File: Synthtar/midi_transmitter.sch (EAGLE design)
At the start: 7 parts, among them IC4 4081N

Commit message: misc changes
misc updates while doing documentation
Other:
- note added: "^ according to the docs I actually do not, cool"
- note added: "need to invert this first! optocoupler inverts on the other side"
- note removed: "according to the docs I actually do not, cool"
- note removed: "need to invert this first!~ optocoupler inverts on the other side"
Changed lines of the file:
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@@
 <text x="93.98" y="10.16" size="1.778" layer="91">thinking about replacing this midi jack with usb midi functionality</text>
 <text x="96.52" y="5.08" size="1.778" layer="97">or having both!</text>
-<text x="20.32" y="43.18" size="1.778" layer="91">need to invert this first!~ optocoupler inverts on the other side</text>
+<text x="20.32" y="48.26" size="1.778" layer="91">need to invert this first! optocoupler inverts on the other side</text>
 <text x="22.86" y="55.88" size="1.778" layer="91">tie all inputs together to avoid floating?</text>
 <text x="68.58" y="-10.16" size="1.778" layer="91">can't drive from nand because my nands can't source enough current!</text>
@@
 <text x="132.08" y="-20.32" size="1.778" layer="91">uses 2.8mA max, 1.7mA avg</text>
 <text x="-10.16" y="68.58" size="1.778" layer="91">just go with what you have for now, you're running out of time</text>
-<text x="20.32" y="45.72" size="1.778" layer="91">according to the docs I actually do not, cool</text>
+<text x="20.32" y="45.72" size="1.778" layer="91">^ according to the docs I actually do not, cool</text>
 <text x="33.02" y="10.16" size="1.778" layer="91">less than 1mA idle current, about 7mA when transmitting</text>
 <text x="33.02" y="7.62" size="1.778" layer="91">(5v-2v)/(220+220 (other side))=6.8mA</text>

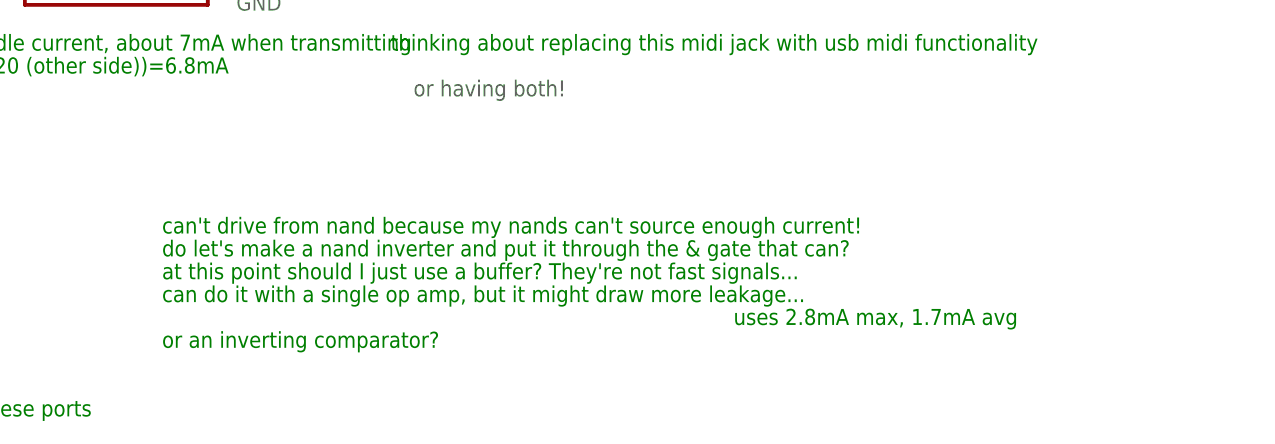
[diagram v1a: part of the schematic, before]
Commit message: deleted some comments
deleted comments in midi trasmitter
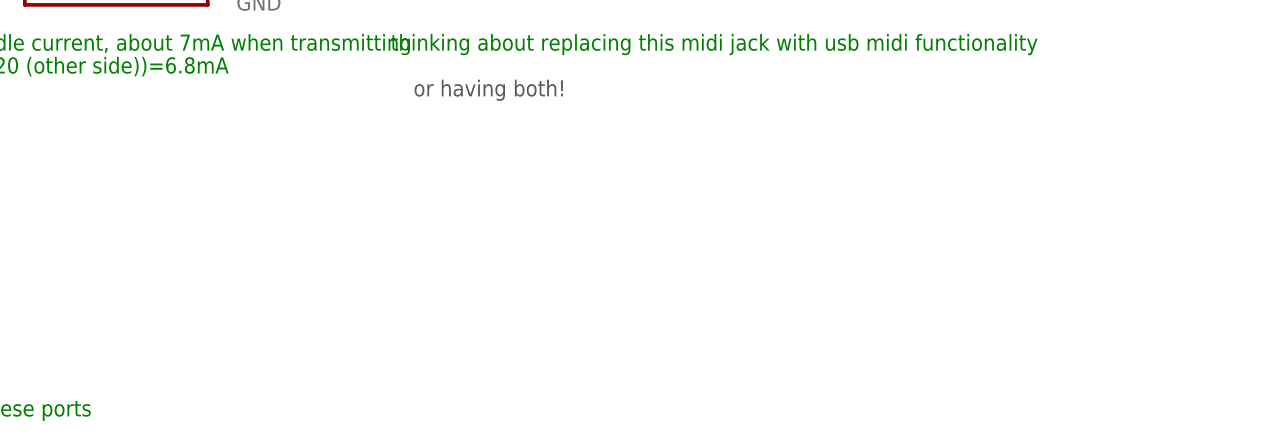
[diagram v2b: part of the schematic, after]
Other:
- note removed: "at this point should I just use a buffer? They're not fast signals..."
- note removed: "can do it with a single op amp, but it might draw more leakage..."
- note removed: "can't drive from nand because my nands can't source enough current!"
- note removed: "do let's make a nand inverter and put it through the & gate that can?"
- note removed: "or an inverting comparator?"
- note removed: "uses 2.8mA max, 1.7mA avg"
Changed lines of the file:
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@@
 <text x="20.32" y="48.26" size="1.778" layer="91">need to invert this first! optocoupler inverts on the other side</text>
 <text x="22.86" y="55.88" size="1.778" layer="91">tie all inputs together to avoid floating?</text>
-<text x="68.58" y="-10.16" size="1.778" layer="91">can't drive from nand because my nands can't source enough current!</text>
-<text x="68.58" y="-12.7" size="1.778" layer="91">do let's make a nand inverter and put it through the &amp; gate that can?</text>
-<text x="68.58" y="-15.24" size="1.778" layer="91">at this point should I just use a buffer? They're not fast signals...</text>
-<text x="68.58" y="-17.78" size="1.778" layer="91">can do it with a single op amp, but it might draw more leakage...</text>
-<text x="68.58" y="-22.86" size="1.778" layer="91">or an inverting comparator?</text>
-<text x="132.08" y="-20.32" size="1.778" layer="91">uses 2.8mA max, 1.7mA avg</text>
 <text x="-10.16" y="68.58" size="1.778" layer="91">just go with what you have for now, you're running out of time</text>
 <text x="20.32" y="45.72" size="1.778" layer="91">^ according to the docs I actually do not, cool</text>
